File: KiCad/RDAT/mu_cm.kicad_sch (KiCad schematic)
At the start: 0 parts

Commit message: Add data from KiCAD and review
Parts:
- added A1: LattePanda_Mu, Module_LattePanda:LattePanda_Module_H8.0mm_Horizontal, symbol MCU_Module_LattePanda:LattePanda_Mu
- added BT2: Battery_Cell, A_HDJ_Library:Battery_Holder_CR1220_S8411-45R, symbol Device:Battery_Cell
- added R8: 1K/1%, symbol Device:R_US
- added SW1: SW_DIP_x03, symbol Switch:SW_DIP_x03
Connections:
- new net: BT2.1 (+), R8.2
- new net: A1.250 (VIN), A1.251 (VIN), A1.252 (VIN), A1.253 (VIN), A1.254 (VIN), A1.255 (VIN), A1.256 (VIN), A1.257 (VIN), A1.258 (VIN), A1.259 (VIN), A1.260 (VIN), SW1.1, SW1.2, SW1.3
- new net: A1.101 (GND), A1.107 (GND), A1.11 (GND), A1.110 (GND), A1.113 (GND), A1.116 (GND), A1.135 (GND), A1.136 (GND), A1.14 (GND), A1.151 (GND), A1.158 (GND), A1.167 (GND), A1.17 (GND), A1.170 (GND), A1.181 (GND), A1.182 (GND), A1.188 (GND), A1.189 (GND), A1.194 (GND), A1.195 (GND), A1.20 (GND), A1.200 (GND), A1.201 (GND), A1.206 (GND), A1.207 (GND), A1.212 (GND), A1.213 (GND), A1.218 (GND), A1.219 (GND), A1.224 (GND), A1.225 (GND), A1.23 (GND), A1.230 (GND), A1.231 (GND), A1.236 (GND), A1.237 (GND), A1.242 (GND), A1.243 (GND), A1.248 (GND), A1.249 (GND), A1.26 (GND), A1.29 (GND), A1.32 (GND), A1.35 (GND), A1.38 (GND), A1.41 (GND), A1.44 (GND), A1.47 (GND), A1.50 (GND), A1.53 (GND), A1.56 (GND), A1.59 (GND), A1.62 (GND), A1.65 (GND), A1.68 (GND), A1.71 (GND), A1.74 (GND), A1.77 (GND), A1.80 (GND), A1.83 (GND), A1.86 (GND), A1.89 (GND), A1.92 (GND), A1.95 (GND), A1.98 (GND)
- new net +15V: SW1.5
- new net +20V: SW1.4
- new net +9V: SW1.6
- new net +BATT: A1.115 (VBAT), R8.1
- new net GND: BT2.2 (-)
- no-connect marks 0 -> 12
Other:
- note added: "3V"

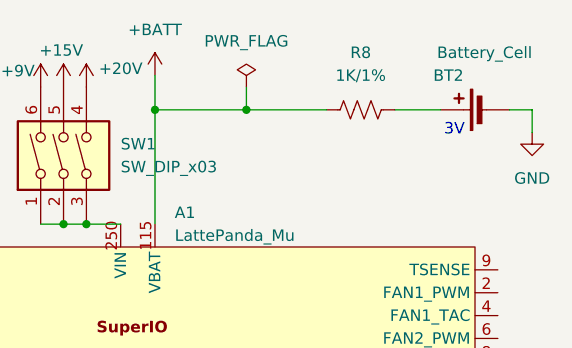
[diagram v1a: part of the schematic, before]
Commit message: Add new notes; update component references in schematics and footprints, and complete charging design
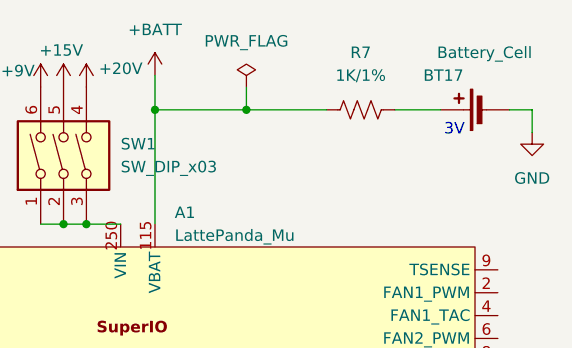
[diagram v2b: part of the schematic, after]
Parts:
- renumbered BT2 to BT17, R8 to R7
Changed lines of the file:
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@@
 		(dnp no)
 		(fields_autoplaced yes)
-		(property "Reference" "#PWR020"
+		(property "Reference" "#PWR021"
 			(at 180.34 58.42 0)
 			(effects
@@
 			(project "RDAT"
 				(path "/0db9370a-8a21-4fd2-83a9-f207c3725dc9/5b2d2e6c-036c-404a-b71b-c732d724c5c0"
-					(reference "#PWR020")
+					(reference "#PWR021")
 					(unit 1)
 				)
@@
 		(on_board yes)
 		(dnp no)
-		(property "Reference" "BT2"
+		(property "Reference" "BT17"
 			(at 172.72 45.72 90)
 			(effects
@@
 			(project "RDAT"
 				(path "/0db9370a-8a21-4fd2-83a9-f207c3725dc9/5b2d2e6c-036c-404a-b71b-c732d724c5c0"
-					(reference "BT2")
+					(reference "BT17")
 					(unit 1)
 				)
@@
 		(on_board yes)
 		(dnp no)
-		(property "Reference" "#PWR016"
+		(property "Reference" "#PWR018"
 			(at 125.73 50.8 0)
 			(effects
@@
 			(project ""
 				(path "/0db9370a-8a21-4fd2-83a9-f207c3725dc9/5b2d2e6c-036c-404a-b71b-c732d724c5c0"
-					(reference "#PWR016")
+					(reference "#PWR018")
 					(unit 1)
 				)
@@
 		(on_board yes)
 		(dnp no)
-		(property "Reference" "#PWR017"
+		(property "Reference" "#PWR019"
 			(at 128.27 50.8 0)
 			(effects
@@
 			(project ""
 				(path "/0db9370a-8a21-4fd2-83a9-f207c3725dc9/5b2d2e6c-036c-404a-b71b-c732d724c5c0"
-					(reference "#PWR017")
+					(reference "#PWR019")
 					(unit 1)
 				)
@@
 		(dnp no)
 		(fields_autoplaced yes)
-		(property "Reference" "#PWR021"
+		(property "Reference" "#PWR017"
 			(at 138.43 49.53 0)
 			(effects
@@
 			(project "RDAT"
 				(path "/0db9370a-8a21-4fd2-83a9-f207c3725dc9/5b2d2e6c-036c-404a-b71b-c732d724c5c0"
-					(reference "#PWR021")
+					(reference "#PWR017")
 					(unit 1)
 				)
@@
 		(on_board yes)
 		(dnp no)
-		(property "Reference" "#PWR018"
+		(property "Reference" "#PWR020"
 			(at 130.81 50.8 0)
 			(effects
@@
 			(project ""
 				(path "/0db9370a-8a21-4fd2-83a9-f207c3725dc9/5b2d2e6c-036c-404a-b71b-c732d724c5c0"
-					(reference "#PWR018")
+					(reference "#PWR020")
 					(unit 1)
 				)
@@
 		(dnp no)
 		(fields_autoplaced yes)
-		(property "Reference" "R8"
+		(property "Reference" "R7"
 			(at 161.29 43.18 90)
 			(effects
@@
 			(project ""
 				(path "/0db9370a-8a21-4fd2-83a9-f207c3725dc9/5b2d2e6c-036c-404a-b71b-c732d724c5c0"
-					(reference "R8")
+					(reference "R7")
 					(unit 1)
 				)

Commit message: added volage stuffs
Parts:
- removed SW1: SW_DIP_x03, symbol Switch:SW_DIP_x03
- added SW1: SW_DPDT_x2, symbol Switch:SW_DPDT_x2
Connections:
- net at A1.250 (VIN), A1.251 (VIN), A1.252 (VIN)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: now also SW1.2 (B)
- new net +10V: SW1.3 (C)
- new net VDC: SW1.1 (A)

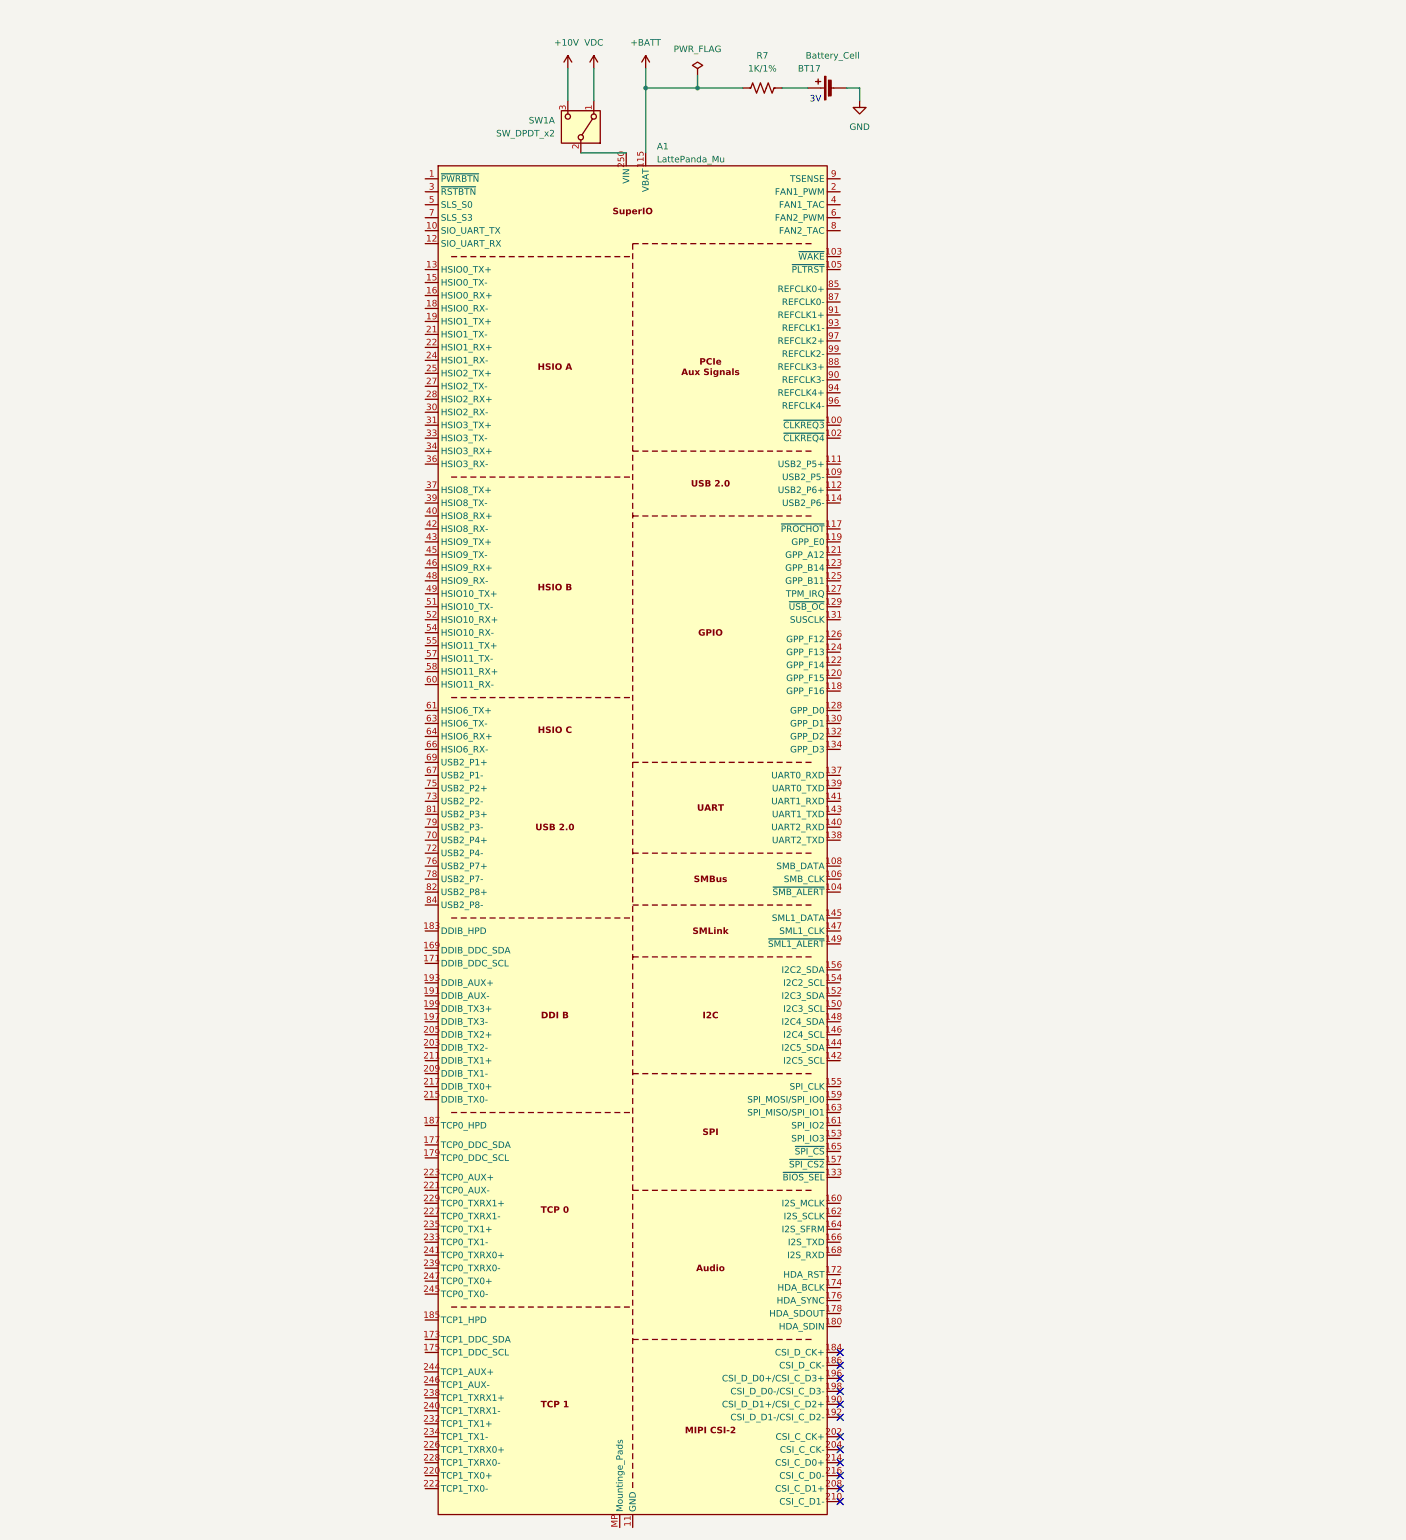
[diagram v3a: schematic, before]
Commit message: Modified Power Stages
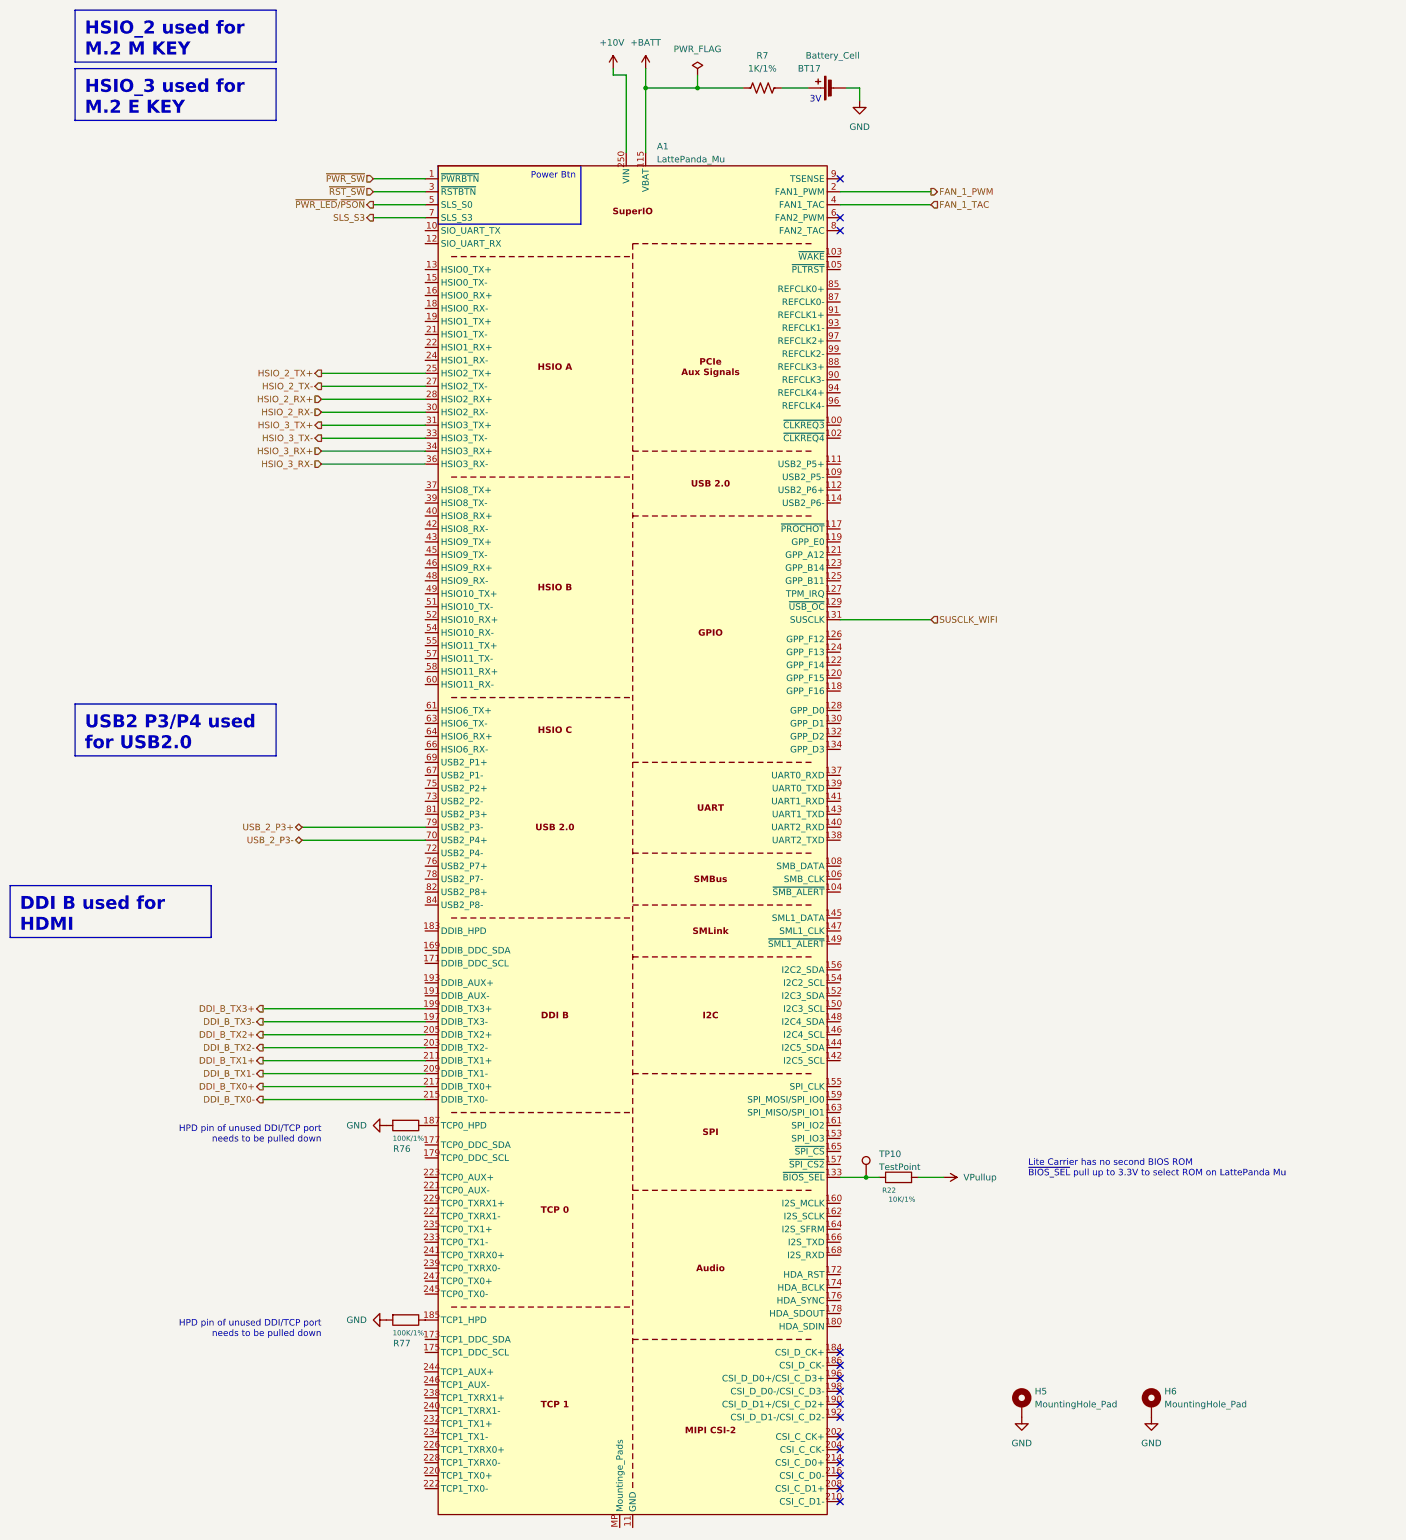
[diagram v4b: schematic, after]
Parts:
- removed SW1: SW_DPDT_x2, symbol Switch:SW_DPDT_x2
- added H5, H6: MountingHole_Pad, A_HDJ_Library:MountingHole_3mm_M2_Pad_TopOnly, symbol Mechanical:MountingHole_Pad
- added R22: 10K/1%, A_HDJ_Library:R_0402_1005Metric, symbol Device:R
- added R76, R77: 100K/1%, A_HDJ_Library:R_0402_1005Metric, symbol Device:R
- added TP10: TestPoint, A_HDJ_Library:TestPoint_Pad_D1.5mm, symbol Connector:TestPoint
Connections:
- net +10V: now also A1.250 (VIN), A1.251 (VIN), A1.252 (VIN), A1.253 (VIN), A1.254 (VIN), A1.255 (VIN), A1.256 (VIN), A1.257 (VIN), A1.258 (VIN), A1.259 (VIN), A1.260 (VIN)
- net GND: now also H5.1, H6.1, R76.2, R77.2
- net ~{PWR_SW}: now reaches A1.1 (~{PWRBTN})
- net SUSCLK_WIFI: now reaches A1.131 (SUSCLK)
- net at A1.133 (~{BIOS_SEL}): now also R22.1, TP10.1
- net at A1.185 (TCP1_HPD): now also R77.1
- net at A1.187 (TCP0_HPD): now also R76.1
- net DDI_B_TX3-: now reaches A1.197 (DDIB_TX3-)
- net DDI_B_TX3+: now reaches A1.199 (DDIB_TX3+)
- net FAN_1_PWM: now reaches A1.2 (FAN1_PWM)
- net DDI_B_TX2-: now reaches A1.203 (DDIB_TX2-)
- net DDI_B_TX2+: now reaches A1.205 (DDIB_TX2+)
- net DDI_B_TX1-: now reaches A1.209 (DDIB_TX1-)
- net DDI_B_TX1+: now reaches A1.211 (DDIB_TX1+)
- net DDI_B_TX0-: now reaches A1.215 (DDIB_TX0-)
- net DDI_B_TX0+: now reaches A1.217 (DDIB_TX0+)
- net HSIO_2_TX+: now reaches A1.25 (HSIO2_TX+)
- net HSIO_2_TX-: now reaches A1.27 (HSIO2_TX-)
- net HSIO_2_RX+: now reaches A1.28 (HSIO2_RX+)
- net ~{RST_SW}: now reaches A1.3 (~{RSTBTN})
- net HSIO_2_RX-: now reaches A1.30 (HSIO2_RX-)
- net HSIO_3_TX+: now reaches A1.31 (HSIO3_TX+)
- net HSIO_3_TX-: now reaches A1.33 (HSIO3_TX-)
- net HSIO_3_RX+: now reaches A1.34 (HSIO3_RX+)
- net HSIO_3_RX-: now reaches A1.36 (HSIO3_RX-)
- net FAN_1_TAC: now reaches A1.4 (FAN1_TAC)
- net ~{PWR_LED}/~{PSON}: now reaches A1.5 (SLS_S0)
- net SLS_S3: now reaches A1.7 (SLS_S3)
- net USB_2_P3-: now reaches A1.70 (USB2_P4+)
- net USB_2_P3+: now reaches A1.79 (USB2_P3-)
- new net VPullup: R22.2
- no-connect marks 12 -> 15
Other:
- note added: "HPD pin of unused DDI/TCP port needs to be pulled down"
- note added: "Lite Carrier has no second BIOS ROM ~{BIOS_SEL} pull up to 3.3V to select ROM on LattePanda Mu"
